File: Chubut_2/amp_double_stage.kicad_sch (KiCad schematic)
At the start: 3 parts, among them J7 In, J8 Out

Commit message: Schematic for the final version
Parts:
- added R17, R18, R19: R, Resistor_SMD:R_0402_1005Metric, symbol Device:R
- J16: renamed from J8; Digikey https://www.digikey.ch/short/n387fprw -> (none)
- renumbered J7 to J15, R1 to R16
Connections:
- net GND: now also R17.1, R19.1
- net Stage_1/Out: now also R17.2, R18.1
- new net Stage_2/In: R18.2, R19.2
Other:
- sheet Stage_1: file amplifying_channel.kicad_sch -> amp_single_stage.kicad_sch
- sheet Stage_2: file amplifying_channel.kicad_sch -> amp_single_stage.kicad_sch
- moved on the sheet: J15, J16, R16

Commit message: First version of final version
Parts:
- renumbered J15 to J13, J16 to J14, R16 to R12, R17 to R13, R18 to R14, R19 to R15
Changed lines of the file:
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@@
   (symbol (lib_id "Connector:Conn_01x01_Male") (at 135.89 100.33 0)
     (in_bom yes) (on_board yes) (fields_autoplaced)
-    (property "Reference" "J15" (id 0) (at 136.525 94.996 0))
+    (property "Reference" "J13" (id 0) (at 136.525 94.996 0))
     (property "Value" "In" (id 1) (at 136.525 97.536 0))
     (property "Footprint" "chubut:MILL-MAX_0965-0-15-20-80-14-11-0" (id 2) (at 135.89 100.33 0)
@@
   (symbol (lib_id "Device:R") (at 184.15 105.41 180)
     (in_bom yes) (on_board yes) (fields_autoplaced)
-    (property "Reference" "R19" (id 0) (at 186.7399 104.1399 0)
+    (property "Reference" "R15" (id 0) (at 186.7399 104.1399 0)
       (effects (font (size 1.27 1.27)) (justify right))
     )
@@
   (symbol (lib_id "Connector:Conn_Coaxial") (at 219.71 100.33 0)
     (in_bom yes) (on_board yes) (fields_autoplaced)
-    (property "Reference" "J16" (id 0) (at 223.012 99.3531 0)
+    (property "Reference" "J14" (id 0) (at 223.012 99.3531 0)
       (effects (font (size 1.27 1.27)) (justify left))
     )
@@
   (symbol (lib_id "Device:R") (at 147.32 105.41 0)
     (in_bom yes) (on_board yes) (fields_autoplaced)
-    (property "Reference" "R16" (id 0) (at 149.352 104.1399 0)
+    (property "Reference" "R12" (id 0) (at 149.352 104.1399 0)
       (effects (font (size 1.27 1.27)) (justify left))
     )
@@
   (symbol (lib_id "power:GND") (at 176.53 109.22 0)
     (in_bom yes) (on_board yes) (fields_autoplaced)
-    (property "Reference" "#PWR038" (id 0) (at 176.53 115.57 0)
+    (property "Reference" "#PWR030" (id 0) (at 176.53 115.57 0)
       (effects (font (size 1.27 1.27)) hide)
     )
@@
   (symbol (lib_id "Device:R") (at 180.34 100.33 90)
     (in_bom yes) (on_board yes) (fields_autoplaced)
-    (property "Reference" "R18" (id 0) (at 180.34 94.4634 90))
+    (property "Reference" "R14" (id 0) (at 180.34 94.4634 90))
     (property "Value" "R" (id 1) (at 180.34 97.0034 90))
     (property "Footprint" "Resistor_SMD:R_0402_1005Metric" (id 2) (at 180.34 102.108 90)
@@
   (symbol (lib_id "power:GND") (at 184.15 109.22 0)
     (in_bom yes) (on_board yes) (fields_autoplaced)
-    (property "Reference" "#PWR039" (id 0) (at 184.15 115.57 0)
+    (property "Reference" "#PWR031" (id 0) (at 184.15 115.57 0)
       (effects (font (size 1.27 1.27)) hide)
     )
@@
   (symbol (lib_id "Device:R") (at 176.53 105.41 180)
     (in_bom yes) (on_board yes) (fields_autoplaced)
-    (property "Reference" "R17" (id 0) (at 179.07 104.1399 0)
+    (property "Reference" "R13" (id 0) (at 179.07 104.1399 0)
       (effects (font (size 1.27 1.27)) (justify right))
     )
@@
   (symbol (lib_id "power:GND") (at 147.32 109.22 0)
     (in_bom yes) (on_board yes) (fields_autoplaced)
-    (property "Reference" "#PWR037" (id 0) (at 147.32 115.57 0)
+    (property "Reference" "#PWR029" (id 0) (at 147.32 115.57 0)
       (effects (font (size 1.27 1.27)) hide)
     )
@@
   (symbol (lib_id "power:GND") (at 219.71 105.41 0)
     (in_bom yes) (on_board yes) (fields_autoplaced)
-    (property "Reference" "#PWR040" (id 0) (at 219.71 111.76 0)
+    (property "Reference" "#PWR032" (id 0) (at 219.71 111.76 0)
       (effects (font (size 1.27 1.27)) hide)
     )

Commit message: Not sure what is this
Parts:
- renumbered J13 to J15, J14 to J16, R12 to R18, R13 to R19, R14 to R20, R15 to R21
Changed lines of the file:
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@@
   (symbol (lib_id "Connector:Conn_01x01_Male") (at 135.89 100.33 0)
     (in_bom yes) (on_board yes) (fields_autoplaced)
-    (property "Reference" "J13" (id 0) (at 136.525 94.996 0))
+    (property "Reference" "J15" (id 0) (at 136.525 94.996 0))
     (property "Value" "In" (id 1) (at 136.525 97.536 0))
     (property "Footprint" "chubut:MILL-MAX_0965-0-15-20-80-14-11-0" (id 2) (at 135.89 100.33 0)
@@
   (symbol (lib_id "Device:R") (at 184.15 105.41 180)
     (in_bom yes) (on_board yes) (fields_autoplaced)
-    (property "Reference" "R15" (id 0) (at 186.7399 104.1399 0)
+    (property "Reference" "R21" (id 0) (at 186.7399 104.1399 0)
       (effects (font (size 1.27 1.27)) (justify right))
     )
@@
   (symbol (lib_id "Connector:Conn_Coaxial") (at 219.71 100.33 0)
     (in_bom yes) (on_board yes) (fields_autoplaced)
-    (property "Reference" "J14" (id 0) (at 223.012 99.3531 0)
+    (property "Reference" "J16" (id 0) (at 223.012 99.3531 0)
       (effects (font (size 1.27 1.27)) (justify left))
     )
@@
   (symbol (lib_id "Device:R") (at 147.32 105.41 0)
     (in_bom yes) (on_board yes) (fields_autoplaced)
-    (property "Reference" "R12" (id 0) (at 149.352 104.1399 0)
+    (property "Reference" "R18" (id 0) (at 149.352 104.1399 0)
       (effects (font (size 1.27 1.27)) (justify left))
     )
@@
   (symbol (lib_id "power:GND") (at 176.53 109.22 0)
     (in_bom yes) (on_board yes) (fields_autoplaced)
-    (property "Reference" "#PWR030" (id 0) (at 176.53 115.57 0)
+    (property "Reference" "#PWR040" (id 0) (at 176.53 115.57 0)
       (effects (font (size 1.27 1.27)) hide)
     )
@@
   (symbol (lib_id "Device:R") (at 180.34 100.33 90)
     (in_bom yes) (on_board yes) (fields_autoplaced)
-    (property "Reference" "R14" (id 0) (at 180.34 94.4634 90))
+    (property "Reference" "R20" (id 0) (at 180.34 94.4634 90))
     (property "Value" "R" (id 1) (at 180.34 97.0034 90))
     (property "Footprint" "Resistor_SMD:R_0402_1005Metric" (id 2) (at 180.34 102.108 90)
@@
   (symbol (lib_id "power:GND") (at 184.15 109.22 0)
     (in_bom yes) (on_board yes) (fields_autoplaced)
-    (property "Reference" "#PWR031" (id 0) (at 184.15 115.57 0)
+    (property "Reference" "#PWR041" (id 0) (at 184.15 115.57 0)
       (effects (font (size 1.27 1.27)) hide)
     )
@@
   (symbol (lib_id "Device:R") (at 176.53 105.41 180)
     (in_bom yes) (on_board yes) (fields_autoplaced)
-    (property "Reference" "R13" (id 0) (at 179.07 104.1399 0)
+    (property "Reference" "R19" (id 0) (at 179.07 104.1399 0)
       (effects (font (size 1.27 1.27)) (justify right))
     )
@@
   (symbol (lib_id "power:GND") (at 147.32 109.22 0)
     (in_bom yes) (on_board yes) (fields_autoplaced)
-    (property "Reference" "#PWR029" (id 0) (at 147.32 115.57 0)
+    (property "Reference" "#PWR039" (id 0) (at 147.32 115.57 0)
       (effects (font (size 1.27 1.27)) hide)
     )
@@
   (symbol (lib_id "power:GND") (at 219.71 105.41 0)
     (in_bom yes) (on_board yes) (fields_autoplaced)
-    (property "Reference" "#PWR032" (id 0) (at 219.71 111.76 0)
+    (property "Reference" "#PWR042" (id 0) (at 219.71 111.76 0)
       (effects (font (size 1.27 1.27)) hide)
     )

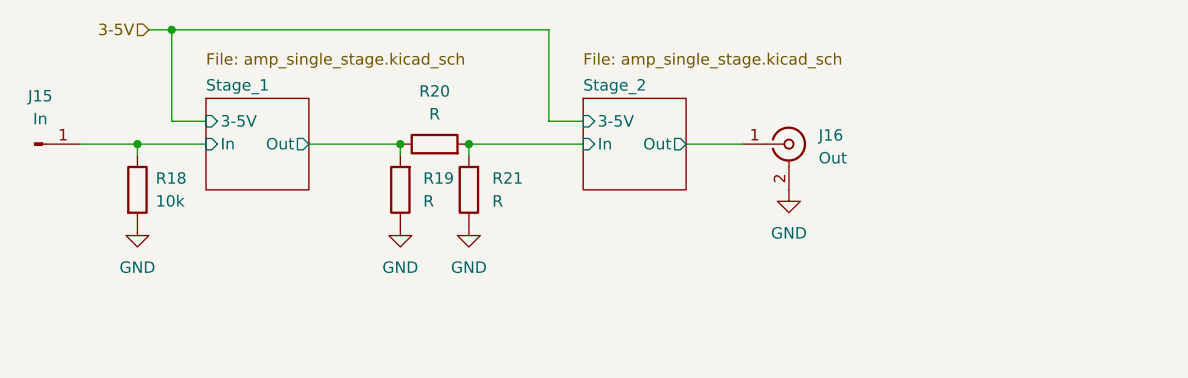
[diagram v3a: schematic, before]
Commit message: Implemented modifications suggested by the workshop
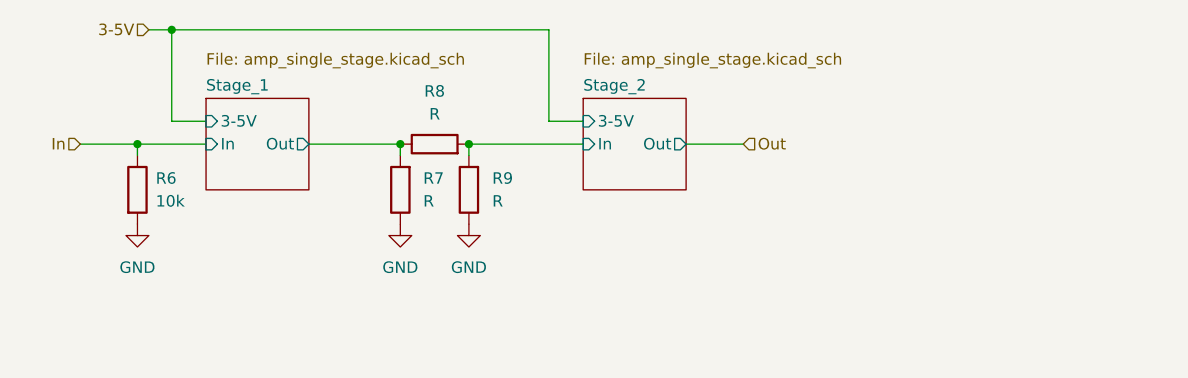
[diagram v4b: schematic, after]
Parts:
- removed J15: In, chubut:MILL-MAX_0965-0-15-20-80-14-11-0, symbol Connector:Conn_01x01_Male
- removed J16: Out, chubut:MMCX-J-P-H-RA-TH1, symbol Connector:Conn_Coaxial
- renumbered R18 to R6, R19 to R7, R20 to R8, R21 to R9
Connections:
- net Stage_1/In renamed In
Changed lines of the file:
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@@
     (stroke (width 0) (type default) (color 0 0 0 0))
+  )
+  (hierarchical_label "Out" (shape input) (at 214.63 100.33 0)
+    (effects (font (size 1.27 1.27)) (justify left))
   )
   (hierarchical_label "3-5V" (shape input) (at 148.59 87.63 180)
     (effects (font (size 1.27 1.27)) (justify right))
   )
-  (symbol (lib_id "Connector:Conn_01x01_Male") (at 135.89 100.33 0)
-    (in_bom yes) (on_board yes) (fields_autoplaced)
-    (property "Reference" "J15" (id 0) (at 136.525 94.996 0))
-    (property "Value" "In" (id 1) (at 136.525 97.536 0))
-    (property "Footprint" "chubut:MILL-MAX_0965-0-15-20-80-14-11-0" (id 2) (at 135.89 100.33 0)
-      (effects (font (size 1.27 1.27)) hide)
-    )
-    (property "Datasheet" "https://www.mill-max.com/products/pin/0965/0965-0-15-20-80-14-11-0?s_term=0965-0-15-20-80-14-11-0&s_type=Quick%2FProduct%2FPart+Number+Search" (id 3) (at 135.89 100.33 0)
-      (effects (font (size 1.27 1.27)) hide)
-    )
-    (property "Manufacturer number" "0965-0-15-20-80-14-11-0" (id 4) (at 135.89 100.33 0)
-      (effects (font (size 1.27 1.27)) hide)
-    )
-    (property "Manufacturer" "Mill-Max Manufacturing Corp." (id 5) (at 135.89 100.33 0)
-      (effects (font (size 1.27 1.27)) hide)
-    )
-    (pin "1")
+  (hierarchical_label "In" (shape input) (at 140.97 100.33 180)
+    (effects (font (size 1.27 1.27)) (justify right))
   )
   (symbol (lib_id "Device:R") (at 184.15 105.41 180)
     (in_bom yes) (on_board yes) (fields_autoplaced)
-    (property "Reference" "R21" (id 0) (at 186.7399 104.1399 0)
+    (property "Reference" "R9" (id 0) (at 186.7399 104.1399 0)
       (effects (font (size 1.27 1.27)) (justify right))
     )
@@
     (pin "2")
   )
-  (symbol (lib_id "Connector:Conn_Coaxial") (at 219.71 100.33 0)
-    (in_bom yes) (on_board yes) (fields_autoplaced)
-    (property "Reference" "J16" (id 0) (at 223.012 99.3531 0)
-      (effects (font (size 1.27 1.27)) (justify left))
-    )
-    (property "Value" "Out" (id 1) (at 223.012 101.8931 0)
-      (effects (font (size 1.27 1.27)) (justify left))
-    )
-    (property "Footprint" "chubut:MMCX-J-P-H-RA-TH1" (id 2) (at 219.71 100.33 0)
-      (effects (font (size 1.27 1.27)) hide)
-    )
-    (property "Datasheet" "http://suddendocs.samtec.com/catalog_english/mmcx.pdf" (id 3) (at 219.71 100.33 0)
-      (effects (font (size 1.27 1.27)) hide)
-    )
-    (property "Manufacturer number" "MMCX-J-P-H-RA-TH1" (id 4) (at 219.71 100.33 0)
-      (effects (font (size 1.27 1.27)) hide)
-    )
-    (property "Manufacturer" "Samtec Inc." (id 5) (at 219.71 100.33 0)
-      (effects (font (size 1.27 1.27)) hide)
-    )
-    (pin "1")
-    (pin "2")
-  )
   (symbol (lib_id "Device:R") (at 147.32 105.41 0)
     (in_bom yes) (on_board yes) (fields_autoplaced)
-    (property "Reference" "R18" (id 0) (at 149.352 104.1399 0)
+    (property "Reference" "R6" (id 0) (at 149.352 104.1399 0)
       (effects (font (size 1.27 1.27)) (justify left))
     )
@@
   (symbol (lib_id "power:GND") (at 176.53 109.22 0)
     (in_bom yes) (on_board yes) (fields_autoplaced)
-    (property "Reference" "#PWR040" (id 0) (at 176.53 115.57 0)
+    (property "Reference" "#PWR023" (id 0) (at 176.53 115.57 0)
       (effects (font (size 1.27 1.27)) hide)
     )
@@
   (symbol (lib_id "Device:R") (at 180.34 100.33 90)
     (in_bom yes) (on_board yes) (fields_autoplaced)
-    (property "Reference" "R20" (id 0) (at 180.34 94.4634 90))
+    (property "Reference" "R8" (id 0) (at 180.34 94.4634 90))
     (property "Value" "R" (id 1) (at 180.34 97.0034 90))
     (property "Footprint" "Resistor_SMD:R_0402_1005Metric" (id 2) (at 180.34 102.108 90)
@@
   (symbol (lib_id "power:GND") (at 184.15 109.22 0)
     (in_bom yes) (on_board yes) (fields_autoplaced)
-    (property "Reference" "#PWR041" (id 0) (at 184.15 115.57 0)
+    (property "Reference" "#PWR024" (id 0) (at 184.15 115.57 0)
       (effects (font (size 1.27 1.27)) hide)
     )
@@
   (symbol (lib_id "Device:R") (at 176.53 105.41 180)
     (in_bom yes) (on_board yes) (fields_autoplaced)
-    (property "Reference" "R19" (id 0) (at 179.07 104.1399 0)
+    (property "Reference" "R7" (id 0) (at 179.07 104.1399 0)
       (effects (font (size 1.27 1.27)) (justify right))
     )
@@
   (symbol (lib_id "power:GND") (at 147.32 109.22 0)
     (in_bom yes) (on_board yes) (fields_autoplaced)
-    (property "Reference" "#PWR039" (id 0) (at 147.32 115.57 0)
+    (property "Reference" "#PWR022" (id 0) (at 147.32 115.57 0)
       (effects (font (size 1.27 1.27)) hide)
     )
@@
       (effects (font (size 1.27 1.27)) hide)
     )
-    (pin "1")
-  )
-  (symbol (lib_id "power:GND") (at 219.71 105.41 0)
-    (in_bom yes) (on_board yes) (fields_autoplaced)
-    (property "Reference" "#PWR042" (id 0) (at 219.71 111.76 0)
-      (effects (font (size 1.27 1.27)) hide)
-    )
-    (property "Value" "GND" (id 1) (at 219.71 110.236 0))
-    (property "Footprint" "" (id 2) (at 219.71 105.41 0)
-      (effects (font (size 1.27 1.27)) hide)
-    )
-    (property "Datasheet" "" (id 3) (at 219.71 105.41 0)
-      (effects (font (size 1.27 1.27)) hide)
-    )

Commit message: Fixed capacitor value
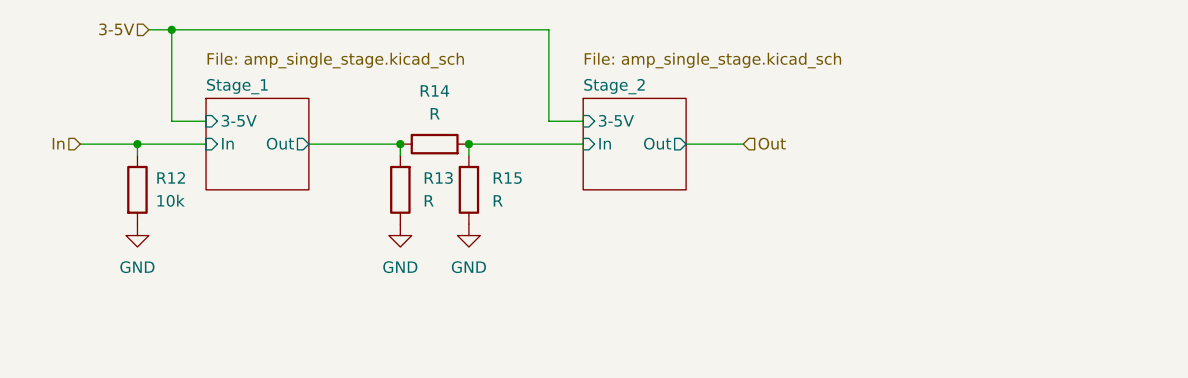
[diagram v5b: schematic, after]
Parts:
- renumbered R6 to R12, R7 to R13, R8 to R14, R9 to R15
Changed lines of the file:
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@@
   (symbol (lib_id "Device:R") (at 184.15 105.41 180)
     (in_bom yes) (on_board yes) (fields_autoplaced)
-    (property "Reference" "R9" (id 0) (at 186.7399 104.1399 0)
+    (property "Reference" "R15" (id 0) (at 186.7399 104.1399 0)
       (effects (font (size 1.27 1.27)) (justify right))
     )
@@
   (symbol (lib_id "Device:R") (at 147.32 105.41 0)
     (in_bom yes) (on_board yes) (fields_autoplaced)
-    (property "Reference" "R6" (id 0) (at 149.352 104.1399 0)
+    (property "Reference" "R12" (id 0) (at 149.352 104.1399 0)
       (effects (font (size 1.27 1.27)) (justify left))
     )
@@
   (symbol (lib_id "power:GND") (at 176.53 109.22 0)
     (in_bom yes) (on_board yes) (fields_autoplaced)
-    (property "Reference" "#PWR023" (id 0) (at 176.53 115.57 0)
+    (property "Reference" "#PWR036" (id 0) (at 176.53 115.57 0)
       (effects (font (size 1.27 1.27)) hide)
     )
@@
   (symbol (lib_id "Device:R") (at 180.34 100.33 90)
     (in_bom yes) (on_board yes) (fields_autoplaced)
-    (property "Reference" "R8" (id 0) (at 180.34 94.4634 90))
+    (property "Reference" "R14" (id 0) (at 180.34 94.4634 90))
     (property "Value" "R" (id 1) (at 180.34 97.0034 90))
     (property "Footprint" "Resistor_SMD:R_0402_1005Metric" (id 2) (at 180.34 102.108 90)
@@
   (symbol (lib_id "power:GND") (at 184.15 109.22 0)
     (in_bom yes) (on_board yes) (fields_autoplaced)
-    (property "Reference" "#PWR024" (id 0) (at 184.15 115.57 0)
+    (property "Reference" "#PWR037" (id 0) (at 184.15 115.57 0)
       (effects (font (size 1.27 1.27)) hide)
     )
@@
   (symbol (lib_id "Device:R") (at 176.53 105.41 180)
     (in_bom yes) (on_board yes) (fields_autoplaced)
-    (property "Reference" "R7" (id 0) (at 179.07 104.1399 0)
+    (property "Reference" "R13" (id 0) (at 179.07 104.1399 0)
       (effects (font (size 1.27 1.27)) (justify right))
     )
@@
   (symbol (lib_id "power:GND") (at 147.32 109.22 0)
     (in_bom yes) (on_board yes) (fields_autoplaced)
-    (property "Reference" "#PWR022" (id 0) (at 147.32 115.57 0)
+    (property "Reference" "#PWR035" (id 0) (at 147.32 115.57 0)
       (effects (font (size 1.27 1.27)) hide)
     )

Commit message: Converted files to KiCAD 7
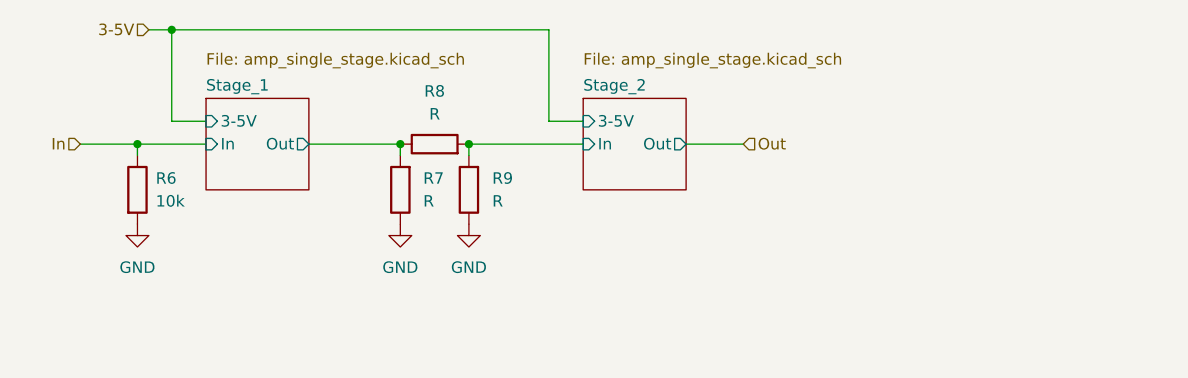
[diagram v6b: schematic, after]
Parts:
- renumbered R12 to R6, R13 to R7, R14 to R8, R15 to R9

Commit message: Added the missing values for the pi attenuator
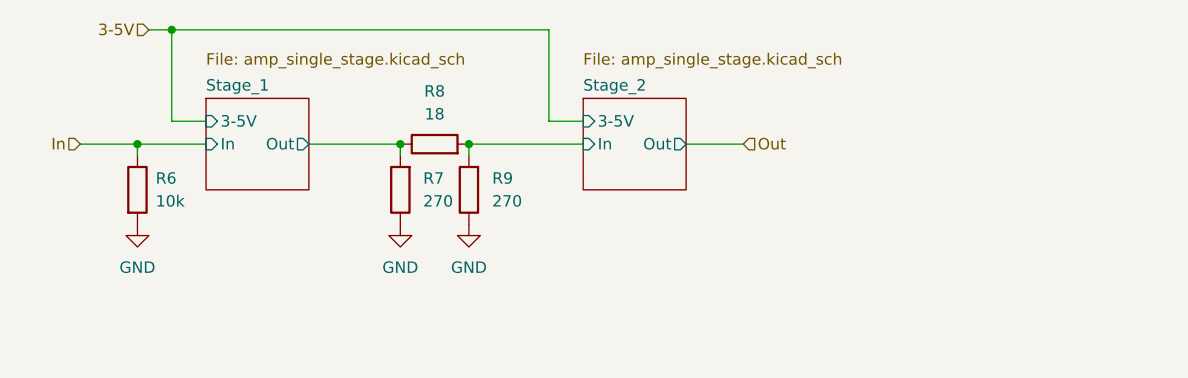
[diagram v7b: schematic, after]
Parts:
- R7, R9: value R -> 270
- R8: value R -> 18
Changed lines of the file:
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@@
       (effects (font (size 1.27 1.27)) (justify right))
     )
-    (property "Value" "R" (at 186.7399 106.6799 0)
+    (property "Value" "270" (at 186.7399 106.6799 0)
       (effects (font (size 1.27 1.27)) (justify right))
     )
@@
       (effects (font (size 1.27 1.27)))
     )
-    (property "Value" "R" (at 180.34 97.0034 90)
+    (property "Value" "18" (at 180.34 97.0034 90)
       (effects (font (size 1.27 1.27)))
     )
@@
       (effects (font (size 1.27 1.27)) (justify right))
     )
-    (property "Value" "R" (at 179.07 106.6799 0)
+    (property "Value" "270" (at 179.07 106.6799 0)
       (effects (font (size 1.27 1.27)) (justify right))
     )
